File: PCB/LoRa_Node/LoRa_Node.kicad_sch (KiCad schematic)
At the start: 72 parts, among them IC1 SPX5205M5-L/TR, J1 Conn_01x04_Socket, J2 Conn_01x02_Pin, J3 UF.L, J4 2x5_2.00mm, J6 Conn_01x06_Socket, J7 Conn_01x03_Socket, SW1 SW_SPST, U1 BME280, U2 RFM95W-868S2, U3 STM32F103C8Tx, U4 SIM800L-CORE, U5 SX1308, Y1 12MHz, Y2 32.768kHz

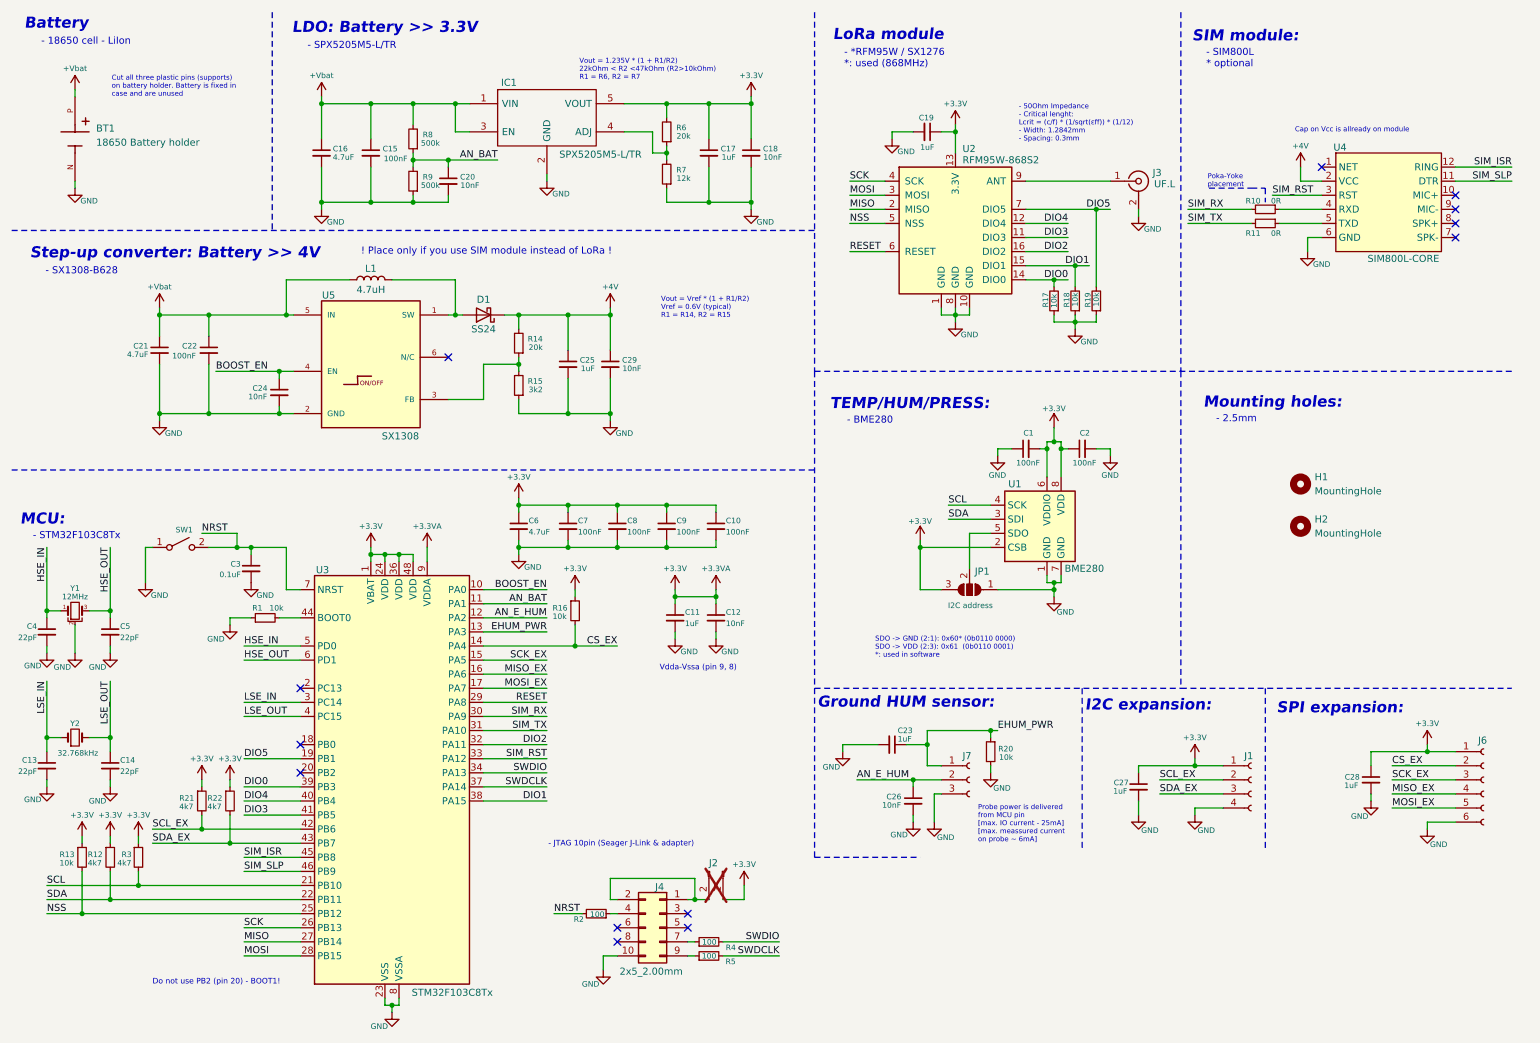
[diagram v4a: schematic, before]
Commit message: PCB modifications, MCU replacement and FW migration
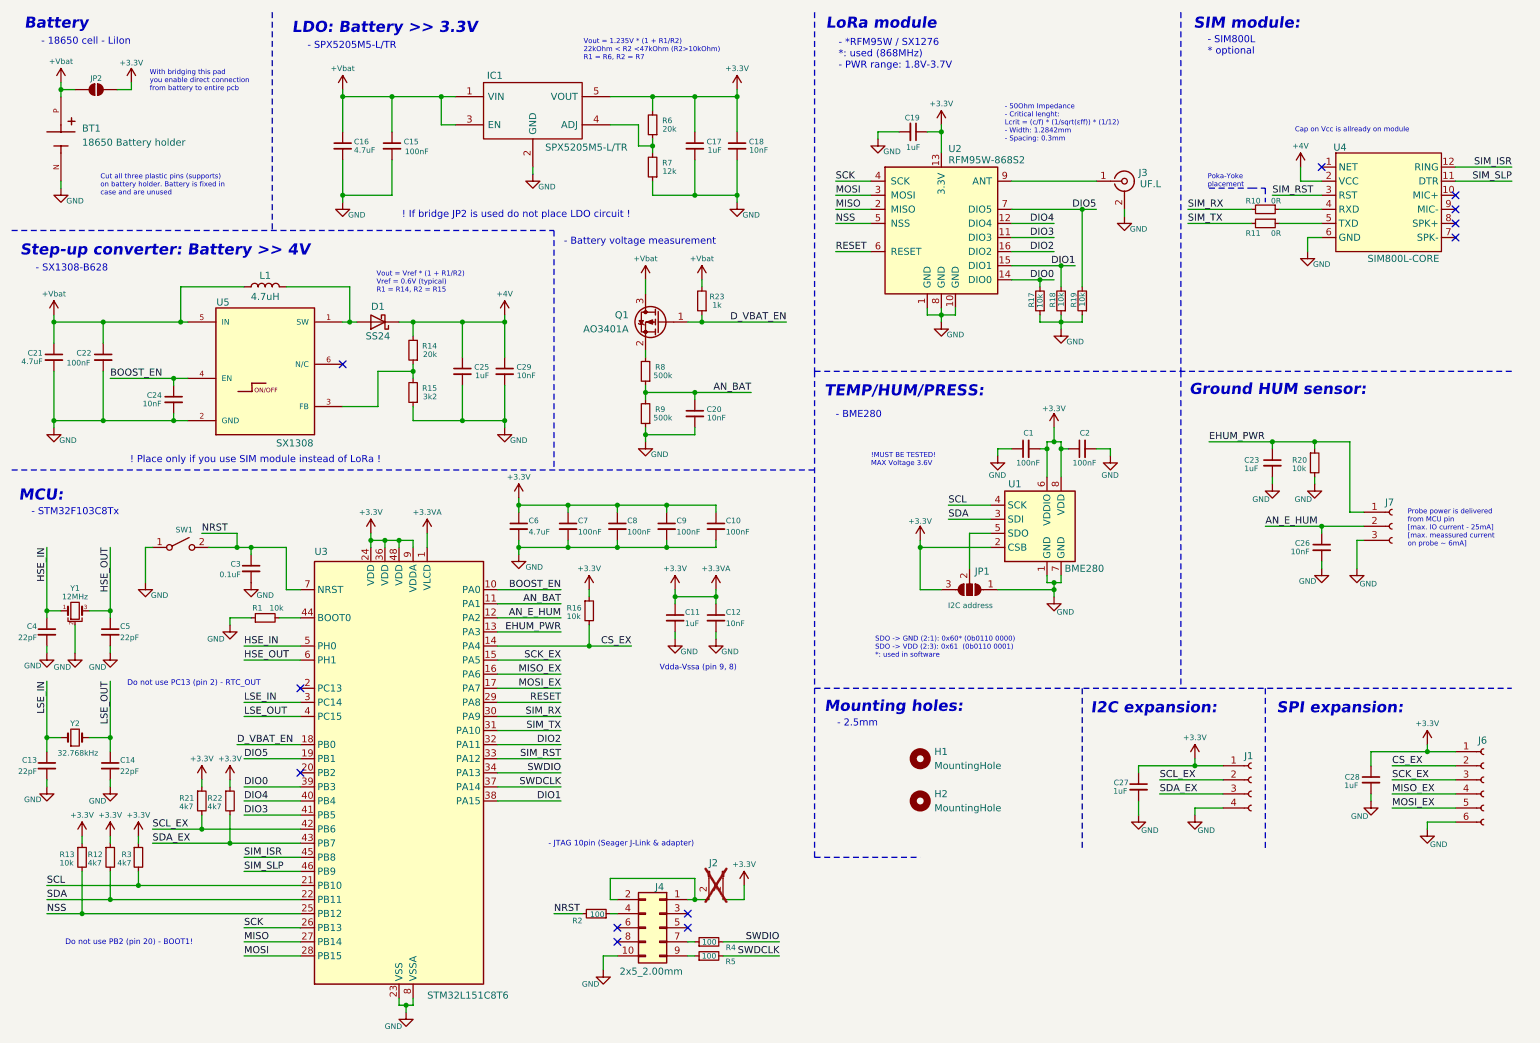
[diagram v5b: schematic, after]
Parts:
- removed U3: STM32F103C8Tx, Package_QFP:LQFP-48_7x7mm_P0.5mm, symbol MCU_ST_STM32F1:STM32F103C8Tx
- added JP2: SolderJumper_2_Open, Jumper:SolderJumper-2_P1.3mm_Open_RoundedPad1.0x1.5mm, symbol Jumper:SolderJumper_2_Open
- added Q1: AO3401A, Package_TO_SOT_SMD:SOT-23, symbol Transistor_FET:AO3401A
- added R23: 1k, Resistor_SMD:R_0603_1608Metric, symbol Device:R_Small
- added U3: STM32L151C8T6, Package_QFP:LQFP-48_7x7mm_P0.5mm, symbol MCU_ST_STM32L1:STM32L151C8Tx
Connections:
- net +3.3V: now also JP2.2 (B), U3.1 (VLCD), U3.24 (VDD), U3.36 (VDD), U3.48 (VDD), U3.9 (VDDA)
- net +Vbat: now also JP2.1 (A), Q1.3 (D), R23.2; no longer R8.2
- net AN_BAT: now also U3.11 (PA1)
- net AN_E_HUM: now also U3.12 (PA2)
- net BOOST_EN: now also U3.10 (PA0)
- net CS_EX: now also U3.14 (PA4)
- net DIO0: now also U3.39 (PB3)
- net DIO1: now also U3.38 (PA15)
- net DIO2: now also U3.32 (PA11)
- net DIO3: now also U3.41 (PB5)
- net DIO4: now also U3.40 (PB4)
- net DIO5: now also U3.19 (PB1)
- net EHUM_PWR: now also U3.13 (PA3)
- net GND: now also U3.23 (VSS), U3.35 (VSS), U3.47 (VSS), U3.8 (VSSA)
- net HSE_IN: now also U3.5 (PH0)
- net HSE_OUT: now also U3.6 (PH1)
- net LSE_IN: now also U3.3 (PC14)
- net LSE_OUT: now also U3.4 (PC15)
- net MISO: now also U3.27 (PB14)
- net MISO_EX: now also U3.16 (PA6)
- net MOSI: now also U3.28 (PB15)
- net MOSI_EX: now also U3.17 (PA7)
- net NRST: now also U3.7 (NRST)
- net NSS: now also U3.25 (PB12)
- net RESET: now also U3.29 (PA8)
- net SCK: now also U3.26 (PB13)
- net SCK_EX: now also U3.15 (PA5)
- net SCL: now also U3.21 (PB10)
- net SCL_EX: now also U3.42 (PB6)
- net SDA: now also U3.22 (PB11)
- net SDA_EX: now also U3.43 (PB7)
- net SIM_ISR: now also U3.45 (PB8)
- net SIM_RST: now also U3.33 (PA12)
- net SIM_RX: now also U3.30 (PA9)
- net SIM_SLP: now also U3.46 (PB9)
- net SIM_TX: now also U3.31 (PA10)
- net SWDCLK: now also U3.37 (PA14)
- net SWDIO: now also U3.34 (PA13)
- net at R1.2: now also U3.44 (BOOT0)
- new net: Q1.2 (S), R8.2
- new net D_VBAT_EN: Q1.1 (G), R23.1, U3.18 (PB0)
- no-connect marks 13 -> 12
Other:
- note added: "! If bridge JP2 is used do not place LDO circuit !"
- note added: "!MUST BE TESTED! MAX Voltage 3.6V"
- note added: "- *RFM95W / SX1276 *: used (868MHz) - PWR range: 1.8V-3.7V"
- note added: "- Battery voltage measurement"
- note added: "Do not use PC13 (pin 2) - RTC_OUT"
- note added: "With bridging this pad you enable direct connection from battery to entire pcb"
- note removed: "- *RFM95W / SX1276 *: used (868MHz)"
- moved on the sheet: BT1, C15, C16, C17, C18, C19, C20, C21, C22, C23, C24, C25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

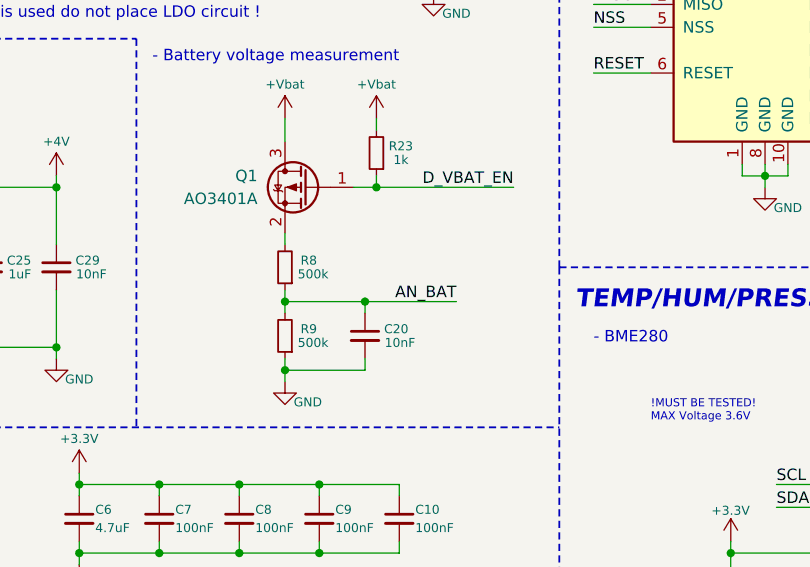
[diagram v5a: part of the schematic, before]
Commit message: ported SW to now MCU - untested
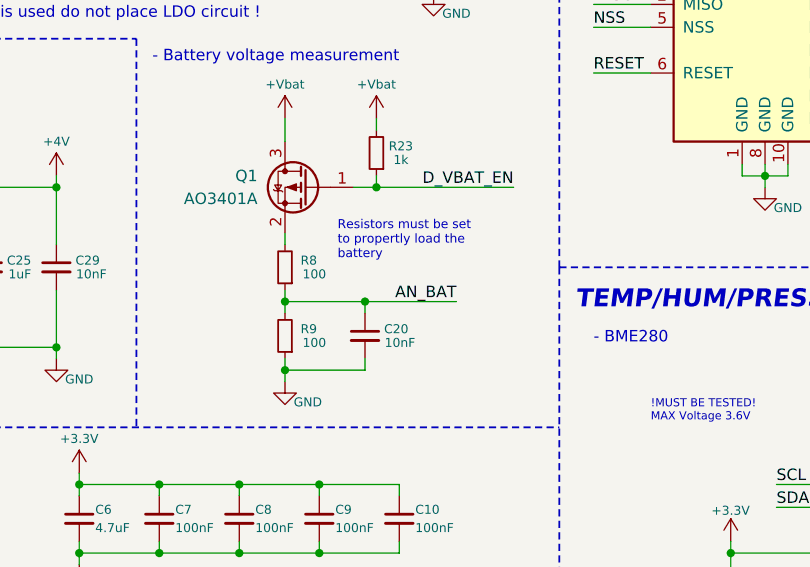
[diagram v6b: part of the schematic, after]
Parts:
- R8, R9: value 500k -> 100
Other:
- note added: "Resistors must be set to propertly load the battery"
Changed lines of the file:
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@@
 		)
 	)
+	(text "Resistors must be set \nto propertly load the\nbattery "
+		(exclude_from_sim no)
+		(at 132.842 77.978 0)
+		(effects
+			(font
+				(size 1 1)
+			)
+			(justify left bottom)
+		)
+	)
 	(text "Vout = Vref * (1 + R1/R2)\nVref = 0.6V (typical)\nR1 = R14, R2 = R15"
 		(exclude_from_sim no)
@@
 			)
 		)
-		(property "Value" "500k"
-			(at 131.826 79.502 0)
+		(property "Value" "100"
+			(at 131.572 79.502 0)
 			(effects
 				(font
@@
 			)
 		)
-		(property "Value" "500k"
-			(at 131.826 87.122 0)
+		(property "Value" "100"
+			(at 131.572 87.122 0)
 			(effects
 				(font

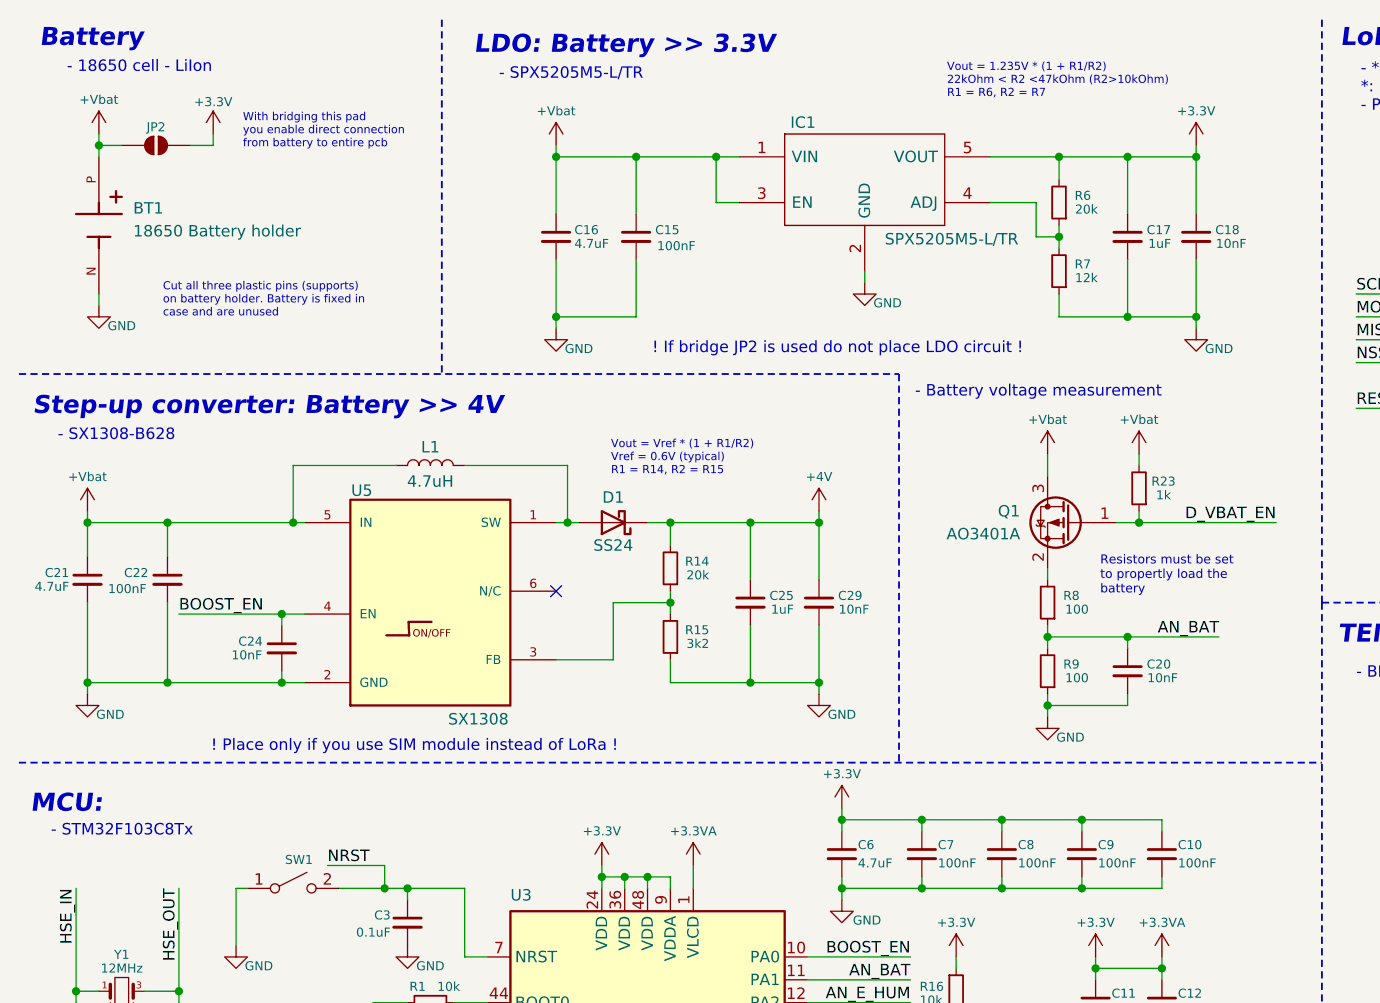
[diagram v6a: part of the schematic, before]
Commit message: update
working code for new mcu, current consumption still 900uA
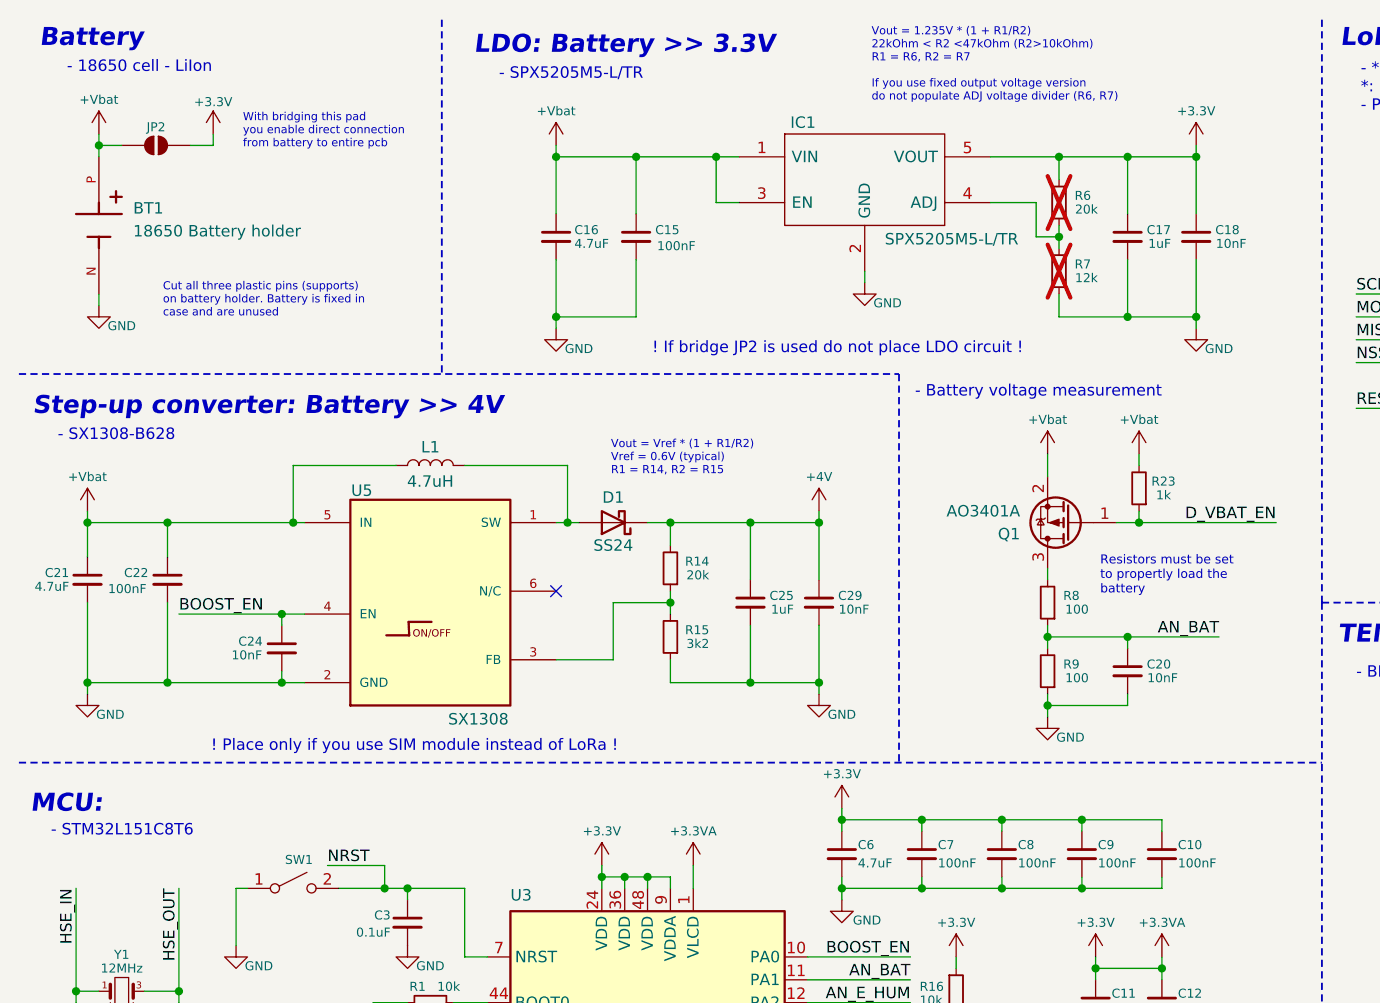
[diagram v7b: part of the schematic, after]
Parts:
- R6, R7: now not fitted
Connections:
- net +Vbat: now also Q1.2 (S); no longer Q1.3 (D)
- net at R8.2: now also Q1.3 (D); no longer Q1.2 (S)
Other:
- note added: "- STM32L151C8T6"
- note added: "Vout = 1.235V * (1 + R1/R2) 22kOhm < R2 <47kOhm (R2>10kOhm) R1 = R6, R2 = R7 If you use fixed output voltage version do not populate ADJ voltage divider (R6, R7)"
- note removed: "- STM32F103C8Tx"
- note removed: "Vout = 1.235V * (1 + R1/R2) 22kOhm < R2 <47kOhm (R2>10kOhm) R1 = R6, R2 = R7"
- moved on the sheet: Q1
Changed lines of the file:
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@@
 	(title_block
 		(title "Greenhouse LoRa node (SIM)")
-		(date "2025-05-24")
-		(rev "4.0")
+		(date "2025-07-20")
+		(rev "4.1")
 		(company "Tinta T.")
 	)
@@
 		)
 	)
-	(text "Vout = 1.235V * (1 + R1/R2)\n22kOhm < R2 <47kOhm (R2>10kOhm)\nR1 = R6, R2 = R7"
+	(text "Vout = 1.235V * (1 + R1/R2)\n22kOhm < R2 <47kOhm (R2>10kOhm)\nR1 = R6, R2 = R7\n\nIf you use fixed output voltage version \ndo not populate ADJ voltage divider (R6, R7)"
 		(exclude_from_sim no)
-		(at 115.824 20.828 0)
+		(at 107.442 19.05 0)
 		(effects
 			(font
@@
 		)
 	)
-	(text "- STM32F103C8Tx"
+	(text "- STM32L151C8T6"
 		(exclude_from_sim no)
 		(at 16.256 104.902 0)
@@
 		(in_bom yes)
 		(on_board yes)
-		(dnp no)
+		(dnp yes)
 		(property "Reference" "R7"
 			(at 131.826 41.148 0)
@@
 	(symbol
 		(lib_id "Transistor_FET:AO3401A")
-		(at 129.54 69.85 0)
-		(mirror y)
+		(at 129.54 69.85 180)
 		(unit 1)
 		(exclude_from_sim no)
@@
 		(dnp no)
 		(property "Reference" "Q1"
-			(at 123.952 68.58 0)
+			(at 123.952 71.12 0)
 			(effects
 				(font
@@
 		)
 		(property "Value" "AO3401A"
-			(at 123.952 71.12 0)
+			(at 123.952 68.58 0)
 			(effects
 				(font
@@
 		)
 		(property "Footprint" "Package_TO_SOT_SMD:SOT-23"
-			(at 124.46 71.755 0)
+			(at 124.46 67.945 0)
 			(effects
 				(font
@@
 		)
 		(property "Datasheet" "http://www.aosmd.com/pdfs/datasheet/AO3401A.pdf"
-			(at 124.46 73.66 0)
+			(at 124.46 66.04 0)
 			(effects
 				(font
@@
 		(in_bom yes)
 		(on_board yes)
-		(dnp no)
+		(dnp yes)
 		(property "Reference" "R6"
 			(at 131.826 33.528 0)
